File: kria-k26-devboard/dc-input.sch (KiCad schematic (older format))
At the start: 3 parts, among them J3 DC_SOCKET

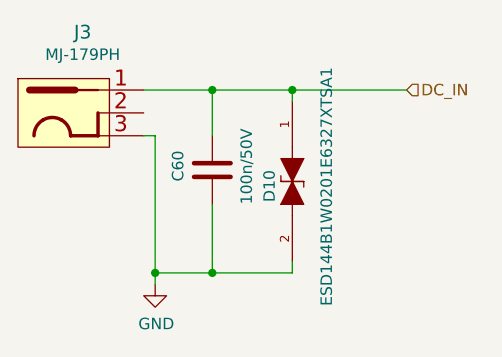
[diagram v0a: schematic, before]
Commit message: Finished reset logic, added crystal gen. to USB PHY, create power toggle for SD 3.0
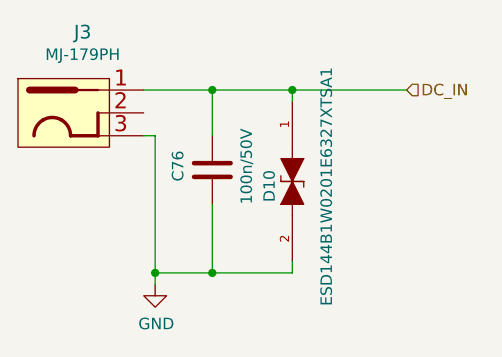
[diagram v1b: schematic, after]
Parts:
- renumbered C60 to C76
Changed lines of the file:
@@
 $Descr A4 11693 8268
 encoding utf-8
-Sheet 9 17
+Sheet 8 17
 Title ""
 Date ""
@@
 P 5750 4350
 AR Path="/63C44BC2/62AA9534" Ref="#PWR?"  Part="1"
-AR Path="/63C44BC2/62AA815B/62AA9534" Ref="#PWR0286"  Part="1"
-F 0 "#PWR0286" H 5750 4100 50  0001 C CNN
+AR Path="/63C44BC2/62AA815B/62AA9534" Ref="#PWR044"  Part="1"
+F 0 "#PWR044" H 5750 4100 50  0001 C CNN
 F 1 "GND" H 5755 4177 50  0000 C CNN
 F 2 "" H 5750 4350 50  0001 C CNN
@@
 P 6000 3850
 AR Path="/63C44BC2/62AA953E" Ref="C?"  Part="1"
-AR Path="/63C44BC2/62AA815B/62AA953E" Ref="C60"  Part="1"
-F 0 "C60" V 5850 3800 50  0000 L CNN
+AR Path="/63C44BC2/62AA815B/62AA953E" Ref="C76"  Part="1"
+F 0 "C76" V 5850 3800 50  0000 L CNN
 F 1 "C_100n_0402_50V" H 6000 3850 50  0001 C CNN
 F 2 "antmicro-footprints:0402-cap" H 6000 3850 50  0001 C CNN

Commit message: Progress in PCB placement
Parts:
- renumbered C76 to C206, D10 to D28, J3 to J11
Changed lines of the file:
@@
 P 5500 3600
 AR Path="/63C44BC2/62AA9529" Ref="J?"  Part="1"
-AR Path="/63C44BC2/62AA815B/62AA9529" Ref="J3"  Part="1"
-F 0 "J3" H 5433 3953 60  0000 C CNN
+AR Path="/63C44BC2/62AA815B/62AA9529" Ref="J11"  Part="1"
+F 0 "J11" H 5433 3953 60  0000 C CNN
 F 1 "DC_SOCKET" H 5550 3325 60  0001 C CNN
 F 2 "antmicro-footprints:DC_SOCKET" H 5550 3250 60  0001 C CNN
@@
 P 5750 4350
 AR Path="/63C44BC2/62AA9534" Ref="#PWR?"  Part="1"
-AR Path="/63C44BC2/62AA815B/62AA9534" Ref="#PWR044"  Part="1"
-F 0 "#PWR044" H 5750 4100 50  0001 C CNN
+AR Path="/63C44BC2/62AA815B/62AA9534" Ref="#PWR0379"  Part="1"
+F 0 "#PWR0379" H 5750 4100 50  0001 C CNN
 F 1 "GND" H 5755 4177 50  0000 C CNN
 F 2 "" H 5750 4350 50  0001 C CNN
@@
 P 6000 3850
 AR Path="/63C44BC2/62AA953E" Ref="C?"  Part="1"
-AR Path="/63C44BC2/62AA815B/62AA953E" Ref="C76"  Part="1"
-F 0 "C76" V 5850 3800 50  0000 L CNN
+AR Path="/63C44BC2/62AA815B/62AA953E" Ref="C206"  Part="1"
+F 0 "C206" V 5850 3800 50  0000 L CNN
 F 1 "C_100n_0402_50V" H 6000 3850 50  0001 C CNN
 F 2 "antmicro-footprints:0402-cap" H 6000 3850 50  0001 C CNN
@@
 P 6350 3900
 AR Path="/63C44BC2/62AA954C" Ref="D?"  Part="1"
-AR Path="/63C44BC2/62AA815B/62AA954C" Ref="D10"  Part="1"
-F 0 "D10" H 6300 3800 50  0000 L CNN
+AR Path="/63C44BC2/62AA815B/62AA954C" Ref="D28"  Part="1"
+F 0 "D28" H 6300 3800 50  0000 L CNN
 F 1 "ESD144B1W0201E6327XTSA1" H 5850 4050 50  0000 L CNN
 F 2 "antmicro-footprints:ESD144B1W0201E6327XTSA1" H 6350 3900 50  0001 C CNN

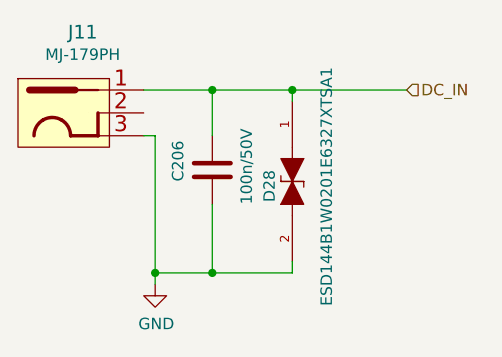
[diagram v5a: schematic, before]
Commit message: Replaced PCIe clock generation (LVDS to HCSL), Clock component size optimization for USB, Optimized ESD protection for PD USB, placed and routed new clock circuitry, clock signals recalculated to 100Ohm  and re-routed
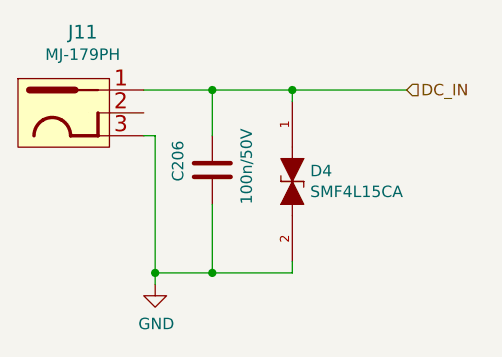
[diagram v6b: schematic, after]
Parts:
- removed D28: ESD144B1W0201E6327XTSA1, antmicro-footprints:ESD144B1W0201E6327XTSA1, symbol antmicroTVSDiodes:ESD144B1W0201E6327XTSA1
- added D4: SMF4L15CA, antmicro-footprints:SOD-123FL, symbol antmicroTVSDiodes:SMF4L15CA
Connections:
- net DC_IN: now also D4.1
- net GND: now also D4.2
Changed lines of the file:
@@
 Wire Wire Line
 	6000 4300 6350 4300
-$Comp
-L antmicroTVSDiodes:ESD144B1W0201E6327XTSA1 D?
-U 1 1 62AA954C
-P 6350 3900
-AR Path="/63C44BC2/62AA954C" Ref="D?"  Part="1"
-AR Path="/63C44BC2/62AA815B/62AA954C" Ref="D28"  Part="1"
-F 0 "D28" H 6300 3800 50  0000 L CNN
-F 1 "ESD144B1W0201E6327XTSA1" H 5850 4050 50  0000 L CNN
-F 2 "antmicro-footprints:ESD144B1W0201E6327XTSA1" H 6350 3900 50  0001 C CNN
-F 3 "https://www.infineon.com/dgdl/Infineon-ESD144-B1-W0201-DataSheet-v02_00-EN.pdf?fileId=5546d462677d0f4601679886a2a8707c" H 6350 3900 50  0001 C CNN
-F 4 "ESD144B1W0201E6327XTSA1" H 6350 3900 50  0001 C CNN "MPN"
-F 5 "Infineon Technologies" H 6350 3900 50  0001 C CNN "Manufacturer"
-	1    6350 3900
-	0    1    1    0
-$EndComp
 Wire Wire Line
 	6350 3550 6350 3500
@@
 Text HLabel 6850 3500 2    50   Input ~ 0
 DC_IN
+$Comp
+L antmicroTVSDiodes:SMF4L15CA D4
+U 1 1 626BB635
+P 6350 3900
+F 0 "D4" V 6304 3978 50  0000 L CNN
+F 1 "SMF4L15CA" V 6395 3978 50  0000 L CNN
+F 2 "antmicro-footprints:SOD-123FL" H 6350 3900 50  0001 C CNN
+F 3 "https://www.mouser.pl/datasheet/2/240/Littelfuse_TVS_Diode_SMF4L_Datasheet_pdf-1665786.pdf" H 6350 3900 50  0001 C CNN
+F 4 "SMF4L15CA" H 6350 3900 50  0001 C CNN "MPN"
+F 5 "Infineon Technologies" H 6350 3900 50  0001 C CNN "Manufacturer"
+	1    6350 3900
+	0    1    1    0
+$EndComp
 $EndSCHEMATC

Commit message: Fixed missing USB - M2 connection, finishing touches of PCB
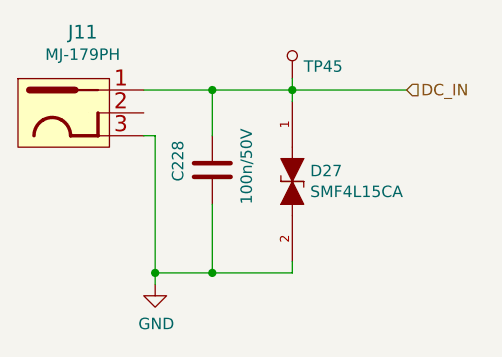
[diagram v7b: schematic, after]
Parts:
- added TP45: TP_SMD_0_75MM, antmicro-footprints:Testpoint_smd_0_75mm, symbol antmicroTestPoints:TP_SMD_0_75MM
- renumbered C206 to C228, D4 to D27
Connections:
- net DC_IN: now also TP45.1
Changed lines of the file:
@@
 P 5750 4350
 AR Path="/63C44BC2/62AA9534" Ref="#PWR?"  Part="1"
-AR Path="/63C44BC2/62AA815B/62AA9534" Ref="#PWR0379"  Part="1"
-F 0 "#PWR0379" H 5750 4100 50  0001 C CNN
+AR Path="/63C44BC2/62AA815B/62AA9534" Ref="#PWR0404"  Part="1"
+F 0 "#PWR0404" H 5750 4100 50  0001 C CNN
 F 1 "GND" H 5755 4177 50  0000 C CNN
 F 2 "" H 5750 4350 50  0001 C CNN
@@
 P 6000 3850
 AR Path="/63C44BC2/62AA953E" Ref="C?"  Part="1"
-AR Path="/63C44BC2/62AA815B/62AA953E" Ref="C206"  Part="1"
-F 0 "C206" V 5850 3800 50  0000 L CNN
+AR Path="/63C44BC2/62AA815B/62AA953E" Ref="C228"  Part="1"
+F 0 "C228" V 5850 3800 50  0000 L CNN
 F 1 "C_100n_0402_50V" H 6000 3850 50  0001 C CNN
 F 2 "antmicro-footprints:0402-cap" H 6000 3850 50  0001 C CNN
@@
 DC_IN
 $Comp
-L antmicroTVSDiodes:SMF4L15CA D4
+L antmicroTVSDiodes:SMF4L15CA D27
 U 1 1 626BB635
 P 6350 3900
-F 0 "D4" V 6304 3978 50  0000 L CNN
+F 0 "D27" V 6304 3978 50  0000 L CNN
 F 1 "SMF4L15CA" V 6395 3978 50  0000 L CNN
 F 2 "antmicro-footprints:SOD-123FL" H 6350 3900 50  0001 C CNN
@@
 	0    1    1    0
 $EndComp
+$Comp
+L antmicroTestPoints:TP_SMD_0_75MM TP45
+U 1 1 63217515
+P 6350 3350
+F 0 "TP45" H 6300 3397 50  0000 R CNN
+F 1 "TP_SMD_0_75MM" H 6350 3250 50  0001 C CNN
+F 2 "antmicro-footprints:Testpoint_smd_0_75mm" H 6550 3550 60  0001 L CNN
+F 3 "" H 6550 3650 60  0001 L CNN
+	1    6350 3350
+	-1   0    0    1
+$EndComp
+Wire Wire Line
+	6350 3500 6350 3450
 $EndSCHEMATC
